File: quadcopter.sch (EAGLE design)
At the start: 98 parts, among them J1 AVR_SPI_PRG_6NS, M1 MOTOR_PADS, M2 MOTOR_PADS, M3 MOTOR_PADS, M4 MOTOR_PADS, Q1 MOSFET_SOT-23, Q2 MOSFET_SOT-23, Q3 MOSFET_SOT-23, Q4 MOSFET_SOT-23, SW1 PUSHBUTTON_SMD-VERTICAL-1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

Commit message: Redesigned board
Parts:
- removed V3: (no value), quadparts_prebuilt:LOCKED-VIA-0.254
- added V2, V35, V36, V4: (no value), custom:VIA_0.454
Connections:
- net 3V: no longer V3.N
- net GND: now also V2.VIA, V35.VIA, V36.VIA, V4.VIA
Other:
- moved on the sheet: V13, V14, V15, V16, V17, V18, V19, V20, V21, V22, V23, V24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

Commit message: Redesigned board and reduced vias
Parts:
- added V3, V37, V38, V39, V40, V41: (no value), quadparts_prebuilt:LOCKED-VIA-0.254
- renumbered SW1 to SW
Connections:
- net 3V: now also V3.N, V37.N
- net BAT_GND: now also V38.N, V39.N, V40.N, V41.N
- net PWM1: now also J3.8; no longer J3.6
- net PWM2: now also J3.4; no longer J3.5
- net PWM3: now also J3.7; no longer J3.4
- net SCL: now also J3.6; no longer J3.8
- net SDA: now also J3.5; no longer J3.7
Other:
- moved on the sheet: V8

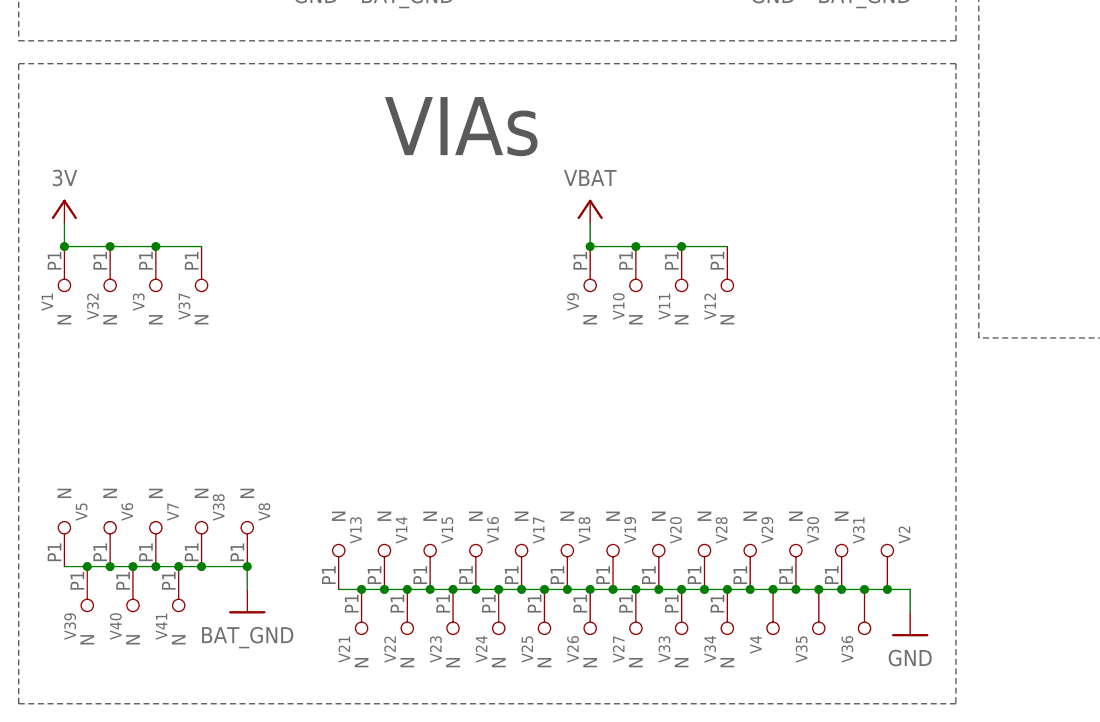
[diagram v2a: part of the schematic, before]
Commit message: Shink motors components and modified pours
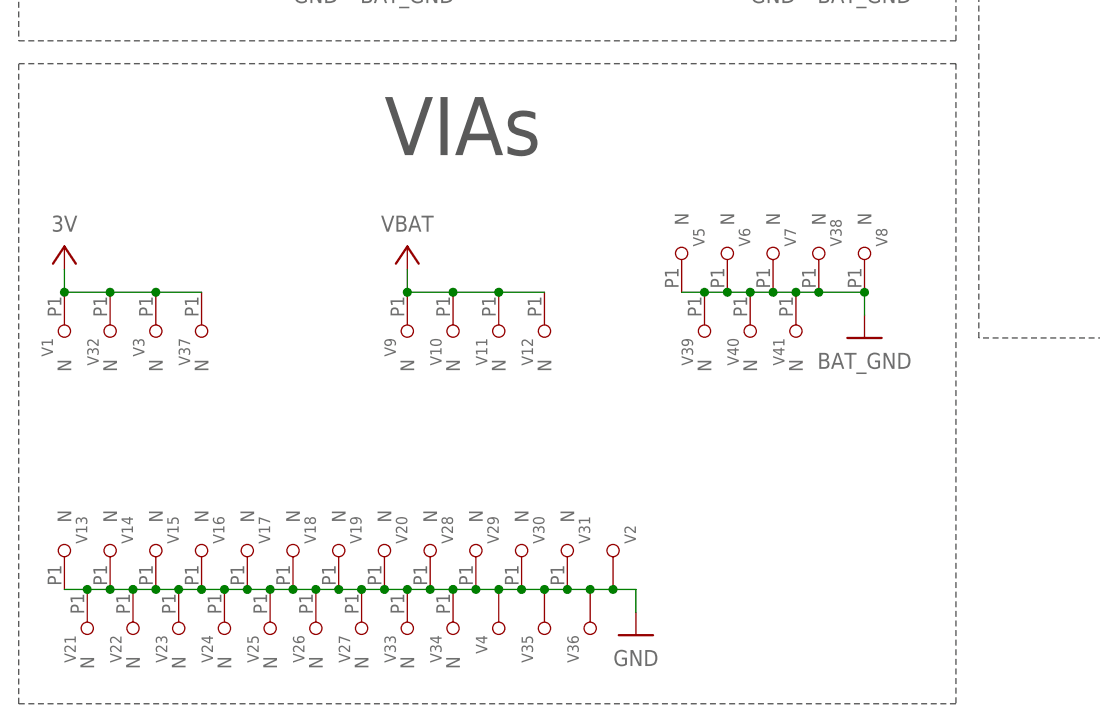
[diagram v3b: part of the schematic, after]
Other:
- moved on the sheet: V1, V10, V11, V12, V13, V14, V15, V16, V17, V18, V19, V2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

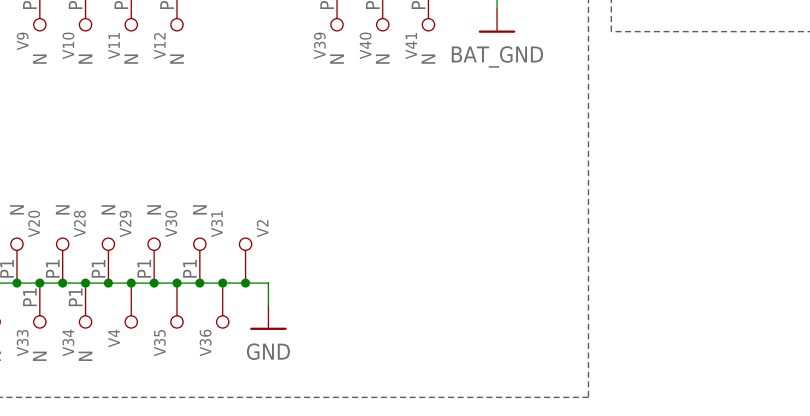
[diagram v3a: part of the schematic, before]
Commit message: Added 2 more vias around antenna driver
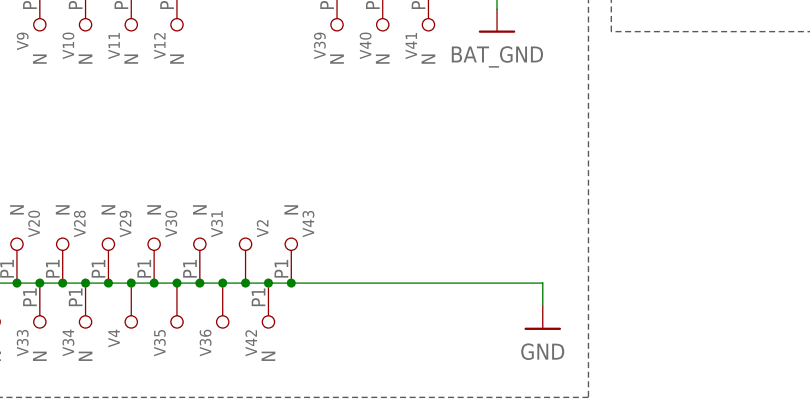
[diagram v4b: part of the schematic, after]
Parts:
- added V42, V43: (no value), quadparts_prebuilt:LOCKED-VIA-0.254
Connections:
- net GND: now also V42.N, V43.N
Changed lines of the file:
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@@
 <part name="V40" library="quadparts_prebuilt" deviceset="LOCKED-VIA" device="-0.254"/>
 <part name="V41" library="quadparts_prebuilt" deviceset="LOCKED-VIA" device="-0.254"/>
+<part name="V42" library="quadparts_prebuilt" deviceset="LOCKED-VIA" device="-0.254"/>
+<part name="V43" library="quadparts_prebuilt" deviceset="LOCKED-VIA" device="-0.254"/>
 </parts>
 <sheets>
@@
 <instance part="V19" gate="G$1" x="60.96" y="30.48" rot="R90"/>
 <instance part="V20" gate="G$1" x="66.04" y="30.48" rot="R90"/>
-<instance part="GND36" gate="1" x="93.98" y="25.4"/>
+<instance part="GND36" gate="1" x="124.46" y="25.4"/>
 <instance part="V21" gate="G$1" x="33.02" y="30.48" rot="R270"/>
 <instance part="V22" gate="G$1" x="38.1" y="30.48" rot="R270"/>
@@
 <instance part="V40" gate="G$1" x="106.68" y="63.5" rot="R270"/>
 <instance part="V41" gate="G$1" x="111.76" y="63.5" rot="R270"/>
+<instance part="V42" gate="G$1" x="93.98" y="30.48" rot="R270"/>
+<instance part="V43" gate="G$1" x="96.52" y="30.48" rot="R90"/>
 </instances>
 <busses>
@@
 <wire x1="88.9" y1="30.48" x2="91.44" y2="30.48" width="0.1524" layer="91"/>
 <wire x1="91.44" y1="30.48" x2="93.98" y2="30.48" width="0.1524" layer="91"/>
-<wire x1="93.98" y1="30.48" x2="93.98" y2="27.94" width="0.1524" layer="91"/>
+<wire x1="93.98" y1="30.48" x2="96.52" y2="30.48" width="0.1524" layer="91"/>
+<wire x1="96.52" y1="30.48" x2="124.46" y2="30.48" width="0.1524" layer="91"/>
+<wire x1="124.46" y1="30.48" x2="124.46" y2="27.94" width="0.1524" layer="91"/>
 <pinref part="V2" gate="G$1" pin="VIA"/>
 <junction x="91.44" y="30.48"/>
@@
 <pinref part="V36" gate="G$1" pin="VIA"/>
 <junction x="88.9" y="30.48"/>
-</segment>
-</net>
+<pinref part="V42" gate="G$1" pin="N"/>
+<junction x="93.98" y="30.48"/>
+<pinref part="V43" gate="G$1" pin="N"/>
+<junction x="96.52" y="30.48"/>
+</segment>
+</net>
